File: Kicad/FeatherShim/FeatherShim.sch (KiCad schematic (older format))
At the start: 3 parts, among them P1 Feather, P2 CONN_01X16, P3 CONN_01X12

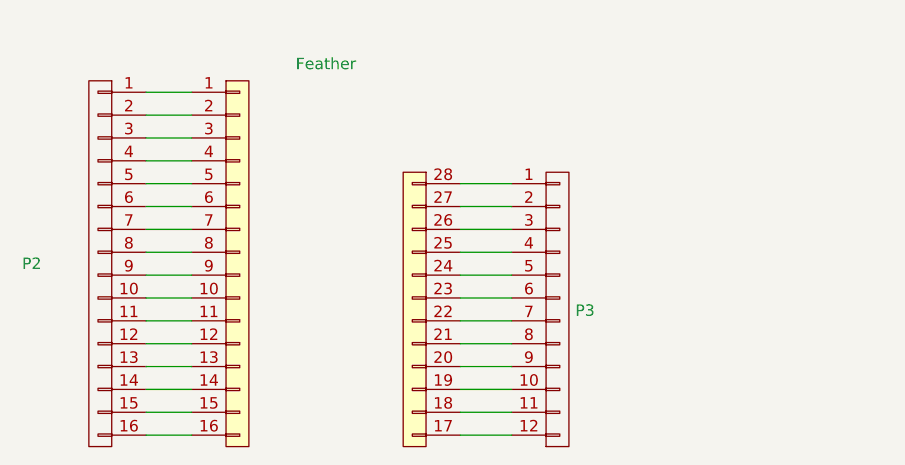
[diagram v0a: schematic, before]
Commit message: thicken power traces
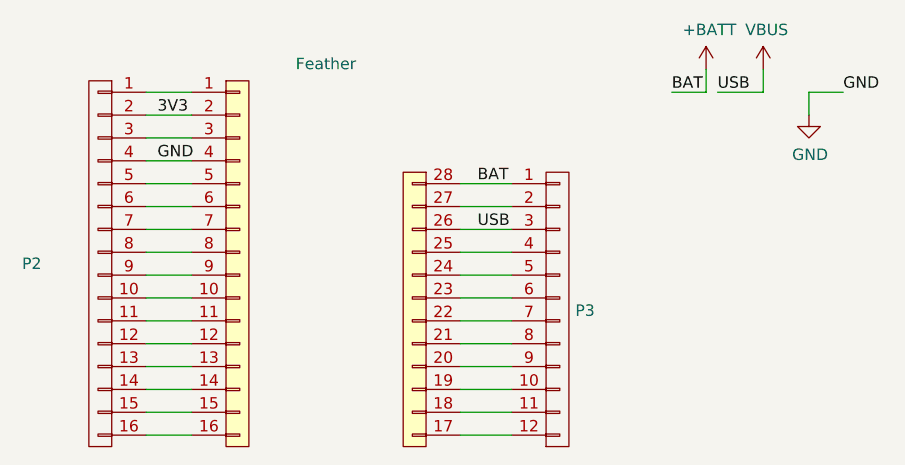
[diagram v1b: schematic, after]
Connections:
- net 3V3: now reaches P1.2 (P2), P2.2 (P2)
- net VBUS: now reaches P1.26 (P26), P3.3 (P3)
- net +BATT: now reaches P1.28 (P28), P3.1 (P1)
- net GND: now reaches P1.4 (P4), P2.4 (P4)
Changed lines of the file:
@@
 Wire Wire Line
 	4575 4250 4800 4250
+Text Label 4650 3150 0    50   ~ 0
+BAT
+Text Label 4650 3350 0    50   ~ 0
+USB
+Text Label 3250 2850 0    50   ~ 0
+3V3
+Text Label 3250 3050 0    50   ~ 0
+GND
+$Comp
+L power:+BATT #PWR?
+U 1 1 5E0A5FE2
+P 5650 2650
+F 0 "#PWR?" H 5650 2500 50  0001 C CNN
+F 1 "+BATT" H 5665 2823 50  0000 C CNN
+F 2 "" H 5650 2650 50  0001 C CNN
+F 3 "" H 5650 2650 50  0001 C CNN
+	1    5650 2650
+	1    0    0    -1
+$EndComp
+$Comp
+L power:GND #PWR?
+U 1 1 5E0A66A3
+P 6100 2850
+F 0 "#PWR?" H 6100 2600 50  0001 C CNN
+F 1 "GND" H 6105 2677 50  0000 C CNN
+F 2 "" H 6100 2850 50  0001 C CNN
+F 3 "" H 6100 2850 50  0001 C CNN
+	1    6100 2850
+	1    0    0    -1
+$EndComp
+$Comp
+L power:VBUS #PWR?
+U 1 1 5E0A72D7
+P 5900 2650
+F 0 "#PWR?" H 5900 2500 50  0001 C CNN
+F 1 "VBUS" H 5915 2823 50  0000 C CNN
+F 2 "" H 5900 2650 50  0001 C CNN
+F 3 "" H 5900 2650 50  0001 C CNN
+	1    5900 2650
+	1    0    0    -1
+$EndComp
+Wire Wire Line
+	6100 2850 6100 2750
+Wire Wire Line
+	6100 2750 6250 2750
+Text Label 6250 2750 0    50   ~ 0
+GND
+Wire Wire Line
+	5650 2650 5650 2750
+Wire Wire Line
+	5650 2750 5500 2750
+Text Label 5500 2750 0    50   ~ 0
+BAT
+Wire Wire Line
+	5900 2650 5900 2750
+Wire Wire Line
+	5900 2750 5700 2750
+Text Label 5700 2750 0    50   ~ 0
+USB
 $EndSCHEMATC
